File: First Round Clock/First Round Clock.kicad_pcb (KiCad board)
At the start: 2 copper layers, 118 x 118 mm, 37 parts, among them J1 PJ-102AH, J2 Conn_01x06, J3 Conn_02x03_Odd_Even, SW1 Omron_B3F_SPST, SW2 Omron_B3F_SPST, SW3 Omron_B3F_SPST, SW4 Omron_B3F_SPST, U1 L7805, U2 ATmega328-PU, U3 DS1307_DIP-8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

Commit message: Week6
All deliverables for week 6
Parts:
- added AmOgUs: LOGO, LOGO, F.Cu at (102.4, 83.6)
- added BZ1: Buzzer, footprints:Buzzer_TDK_PS1240P02BT_D12.2mm_H6.5mm, B.Cu at (198.0, 88.0)
- added G***: LOGO, footprints:HPS_logo, F.Cu at (174.0, 140.0)
- added LeThs GoOoO: LOGO, LOGO, B.Cu at (113.3, 120.9)
- added Q1: NPN_2N3904_SOT23, footprints:SOT-23, F.Cu at (193.0, 99.0)
- added R12: R_0805_10K, footprints:R_0805_2012Metric, F.Cu at (152.7, 123.7)
- added R13: R_0805_10K, footprints:R_0805_2012Metric, F.Cu at (136.0, 124.0)
- added R14: R_0805_10K, footprints:R_0805_2012Metric, F.Cu at (157.5, 124.0)
- added SW5: Omron_B3F_SPST, footprints:SW_SPST_Omron_B3FS-100xP, F.Cu at (191.0, 115.0)
- BT1, RV1: moved to B.Cu
- J1: value PJ-102AH -> Power_inlet_vertical; footprint footprints:PJ-102AH -> footprints:Wurth-694106402002; moved to B.Cu
- R10: value R_0805_10K -> R_0805_100K
- R5: value R_0805_2.2K -> R_0805_1K
- R6: value R_0805_10K -> R_0805_2.2K
- R7: value PhotoconductivePhotocell -> R_0805_10K; footprint footprints:R_LDR_4.9x4.2mm_P2.54mm_Vertical -> footprints:R_0805_2012Metric
- R8: value R_0805_100K -> R_0805_1K
- R9: value R_0805_10K -> PhotoconductivePhotocell; footprint footprints:R_0805_2012Metric -> footprints:R_LDR_4.9x4.2mm_P2.54mm_Vertical
- U1: footprint footprints:TO-220-3_Vertical -> footprints:TO-252-2
- moved U1 91.7 mm to (133.0, 142.0)
- moved R9 87.8 mm to (151.7, 54.0)
- moved C4 84.1 mm to (142.0, 136.0)
- moved C3 81.0 mm to (142.0, 145.0), turned to 90 degrees
- moved R3 75.3 mm to (169.0, 124.0), turned to 90 degrees
- moved R4 73.8 mm to (165.0, 124.0), turned to -90 degrees
- moved J1 73.5 mm to (150.0, 145.0)
- moved R5 69.1 mm to (198.0, 96.0), turned to 0 degrees
- moved R7 63.7 mm to (181.0, 116.0), turned to 90 degrees
- moved U2 59.2 mm to (167.5, 112.2), turned to -90 degrees
- moved R8 52.6 mm to (186.0, 107.0), turned to 0 degrees
- moved SW4 50.1 mm to (118.0, 128.0), turned to 180 degrees
- moved R11 39.5 mm to (132.0, 124.0), turned to 90 degrees
- moved C2 39.2 mm to (153.0, 109.0), turned to -90 degrees
- moved C6 38.0 mm to (135.0, 108.0), turned to -90 degrees
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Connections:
- R10 pad 1: VCC -> LIGHT_SENSOR
- R10 pad 2: BTN_SELECT -> GND
- R11 pad 2: BTN_UP -> BTN_MODE
- R5 pad 1: Net-(D1-Pad1) -> VCC
- R5 pad 2: GND -> Net-(BZ1-Pad2)
- R6 pad 1: VCC -> Net-(D1-Pad1)
- R6 pad 2: RESET -> GND
- R7 pad 2: LIGHT_SENSOR -> RESET
- R8 pad 1: LIGHT_SENSOR -> Buzz
- R8 pad 2: GND -> Net-(Q1-Pad1)
- R9 pad 2: BTN_MODE -> LIGHT_SENSOR
- SW3 pad 3: BTN_SELECT -> BTN_DWN
- SW3 pad 4: BTN_SELECT -> BTN_DWN
- SW4 pad 3: BTN_UP -> BTN_SELECT
- SW4 pad 4: BTN_UP -> BTN_SELECT
- U2 pad 11: LCD_11 -> LCD_12
- U2 pad 12: LCD_12 -> LCD_11
- U2 pad 13: LCD_13 -> LCD_6
- U2 pad 14: LCD_14 -> LCD_4
- U2 pad 15: LCD_4 -> BTN_MODE
- U2 pad 16: LCD_6 -> BTN_SELECT
- U2 pad 23: Light_Sensor -> BTN_DWN
- U2 pad 24: unconnected-(U2-Pad24) -> BTN_UP
- U2 pad 26: unconnected-(U2-Pad26) -> LIGHT_SENSOR
- U2 pad 4: BTN_MODE -> Buzz
- U2 pad 5: BTN_SEL -> LCD_14
- U2 pad 6: BTN_UP -> LCD_13
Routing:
- net GND: track 0.00 -> 265.3 mm
- net SCL: track 0.00 -> 146.9 mm
- net SDA: track 0.00 -> 132.2 mm
- net LIGHT_SENSOR: track 0.00 -> 84.4 mm
- net LED_SCK: track 0.00 -> 64.6 mm
- net MOSI: track 0.00 -> 61.3 mm
- net BTN_DWN: track 0.00 -> 60.7 mm
- net BTN_UP: track 0.00 -> 57.6 mm
- net MISO: track 0.00 -> 52.4 mm
- net LCD_11: track 0.00 -> 51.4 mm
- net LCD_4: track 0.00 -> 50.0 mm
- net LCD_6: track 0.00 -> 46.8 mm
- net LCD_14: track 0.00 -> 46.1 mm
- net LCD_13: track 0.00 -> 44.1 mm
- net LCD_12: track 0.00 -> 43.0 mm
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- added copper zone on B.Cu, net GND
- added copper zone on F.Cu, net VCC
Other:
- board text added: "Andrew Perez's really cool and epic clock"

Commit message: Final clock
Final gerber out for clock
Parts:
- added TP1: TestPoint, footprints:TestPoint_THTPad_D2.0mm_Drill1.0mm, F.Cu at (203.2, 92.7)
- added TP10: TestPoint, footprints:TestPoint_THTPad_D2.0mm_Drill1.0mm, F.Cu at (157.5, 57.1)
- added TP11: TestPoint, footprints:TestPoint_THTPad_D2.0mm_Drill1.0mm, F.Cu at (111.8, 64.8)
- added TP12: TestPoint, footprints:TestPoint_THTPad_D2.0mm_Drill1.0mm, F.Cu at (146.2, 128.5)
- added TP14: TestPoint, footprints:TestPoint_THTPad_D2.0mm_Drill1.0mm, F.Cu at (180.5, 132.0)
- added TP15: TestPoint, footprints:TestPoint_THTPad_D2.0mm_Drill1.0mm, F.Cu at (129.5, 64.8)
- added TP16: TestPoint, footprints:TestPoint_THTPad_D2.0mm_Drill1.0mm, F.Cu at (133.3, 50.8)
- added TP2: TestPoint, footprints:TestPoint_THTPad_D2.0mm_Drill1.0mm, F.Cu at (128.3, 115.6)
- added TP3: TestPoint, footprints:TestPoint_THTPad_D2.0mm_Drill1.0mm, F.Cu at (139.7, 148.6)
- added TP5: TestPoint, footprints:TestPoint_THTPad_D2.0mm_Drill1.0mm, F.Cu at (148.6, 62.2)
- added TP6: TestPoint, footprints:TestPoint_THTPad_D2.0mm_Drill1.0mm, F.Cu at (186.7, 63.5)
- added TP7: TestPoint, footprints:TestPoint_THTPad_D2.0mm_Drill1.0mm, F.Cu at (138.4, 132.1)
- added TP8: TestPoint, footprints:TestPoint_THTPad_D2.0mm_Drill1.0mm, F.Cu at (174.0, 125.7)
- added TP9: TestPoint, footprints:TestPoint_THTPad_D2.0mm_Drill1.0mm, F.Cu at (194.3, 105.4)
- moved D1 2.70 mm to (140.3, 123.7)
- moved R6 1.86 mm to (144.0, 124.5)
- moved C5 1.44 mm to (147.2, 124.3)
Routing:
- net MOSI: track 61.3 -> 128.1 mm
- net LIGHT_SENSOR: track 84.4 -> 125.4 mm
- net GND: track 265.3 -> 293.5 mm
- net Net-(C2-Pad2): track 9.57 -> 32.1 mm
- net LED_SCK: track 64.6 -> 76.5 mm
- net Net-(DS1-Pad3): track 8.01 -> 19.8 mm
- net Net-(U3-Pad1): track 3.28 -> 11.5 mm
- net SCL: track 146.9 -> 154.9 mm
- net BTN_DWN: track 60.7 -> 55.1 mm
- net Net-(C3-Pad1): track 10.3 -> 13.9 mm
- net MISO: track 52.4 -> 49.1 mm
- net SDA: track 132.2 -> 135.5 mm
- net BTN_UP: track 57.6 -> 54.8 mm
- net RESET: track 36.0 -> 38.7 mm
- net Net-(BT1-Pad1): track 34.5 -> 36.9 mm
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
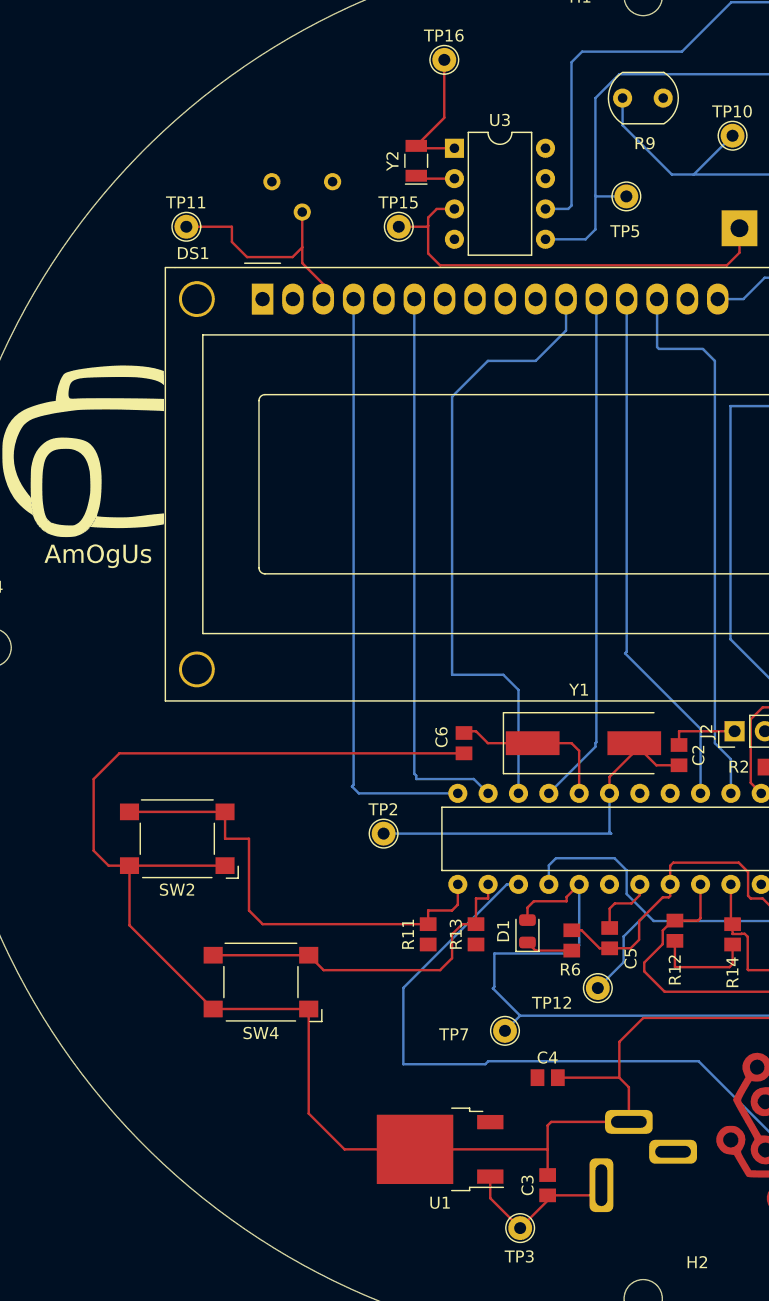
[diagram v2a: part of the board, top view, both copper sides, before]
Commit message: final fix for clock
Final clock used and fixed
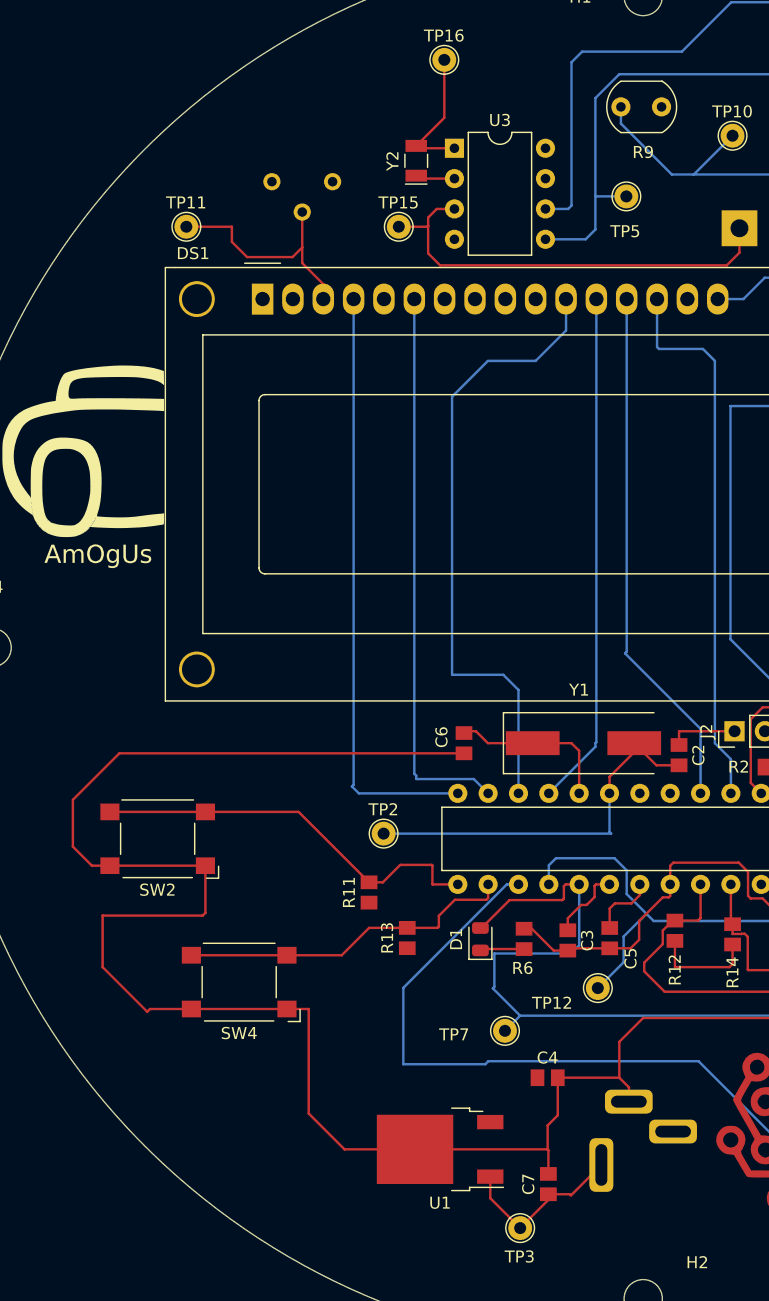
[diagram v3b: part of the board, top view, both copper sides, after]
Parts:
- added C7: C_0805_1uf, footprints:C_0805_2012Metric, F.Cu at (142.1, 144.9)
- moved C3 20.6 mm to (143.7, 124.5), turned to -90 degrees
- moved R11 6.06 mm to (127.1, 120.5)
- moved R13 5.76 mm to (130.3, 124.3)
- moved D1 3.99 mm to (136.4, 124.4)
- moved R6 3.99 mm to (140.0, 124.4)
- moved SW4 1.82 mm to (116.2, 128.0)
- moved J1 1.69 mm to (150.0, 143.3)
- moved SW2 1.64 mm to (109.4, 116.0)
- moved R9 0.75 mm to (151.5, 54.7)
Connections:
- C3 pad 1: Net-(C3-Pad1) -> VCC
- J1 pad 1: Net-(C3-Pad1) -> Net-(J1-Pad1)
- TP3 pad 1: Net-(C3-Pad1) -> Net-(J1-Pad1)
- U1 pad 1: Net-(C3-Pad1) -> Net-(J1-Pad1)
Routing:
- net Net-(J1-Pad1): track 0.00 -> 14.7 mm
- net Net-(C3-Pad1): track 13.9 -> 0.00 mm
- net GND: track 293.5 -> 306.9 mm
- net VCC: track 8.77 -> 15.0 mm
- net BTN_MODE: track 39.3 -> 33.8 mm
- net LED_SCK: track 76.5 -> 80.5 mm
- net BTN_SELECT: track 29.6 -> 28.5 mm
- net LIGHT_SENSOR: track 125.4 -> 124.7 mm
